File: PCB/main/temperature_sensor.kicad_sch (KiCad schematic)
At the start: 6 parts, among them Q1 FDS6690A, U1 MCP9700T-ETT

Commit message: Add sheet properties
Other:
- company: (none) -> University of Cape Town
- title: (none) -> Temperature Sensor
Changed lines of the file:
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@@
 (kicad_sch (version 20211123) (generator eeschema)
   (paper "A4")
+  (title_block
+    (title "Temperature Sensor")
+    (date "2022-03-09")
+    (rev "v1.0")
+    (company "University of Cape Town")
+    (comment 4 "Author: Kelvin Yankey")
+  )
   (junction (at 114.3 135.89) (diameter 0) (color 0 0 0 0)
   )

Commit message: Add changes
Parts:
- renumbered D4 to D10, R8 to R14, R10 to R15, R11 to R16, U1 to U7
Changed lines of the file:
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@@
   (symbol (lib_id "Device:R") (at 186.69 86.36 0) (unit 1)
     (in_bom yes) (on_board yes) (fields_autoplaced)
-    (property "Reference" "R11" (id 0) (at 189.23 85.0899 0)
+    (property "Reference" "R16" (id 0) (at 189.23 85.0899 0)
       (effects (font (size 1.27 1.27)) (justify left))
     )
@@
   (symbol (lib_id "Device:LED") (at 186.69 99.06 90) (unit 1)
     (in_bom yes) (on_board yes) (fields_autoplaced)
-    (property "Reference" "D4" (id 0) (at 190.5 99.3774 90)
+    (property "Reference" "D10" (id 0) (at 190.5 99.3774 90)
       (effects (font (size 1.27 1.27)) (justify right))
     )
@@
   (symbol (lib_id "Sensor_Temperature:MCP9700T-ETT") (at 165.1 74.93 0) (unit 1)
     (in_bom yes) (on_board yes) (fields_autoplaced)
-    (property "Reference" "U1" (id 0) (at 156.21 73.6599 0)
+    (property "Reference" "U7" (id 0) (at 156.21 73.6599 0)
       (effects (font (size 1.27 1.27)) (justify right))
     )
@@
   (symbol (lib_id "Device:R") (at 146.05 41.91 0) (unit 1)
     (in_bom yes) (on_board yes) (fields_autoplaced)
-    (property "Reference" "R8" (id 0) (at 148.59 40.6399 0)
+    (property "Reference" "R14" (id 0) (at 148.59 40.6399 0)
       (effects (font (size 1.27 1.27)) (justify left))
     )
@@
   (symbol (lib_id "Device:R") (at 146.05 53.34 0) (unit 1)
     (in_bom yes) (on_board yes) (fields_autoplaced)
-    (property "Reference" "R10" (id 0) (at 148.59 52.0699 0)
+    (property "Reference" "R15" (id 0) (at 148.59 52.0699 0)
       (effects (font (size 1.27 1.27)) (justify left))
     )

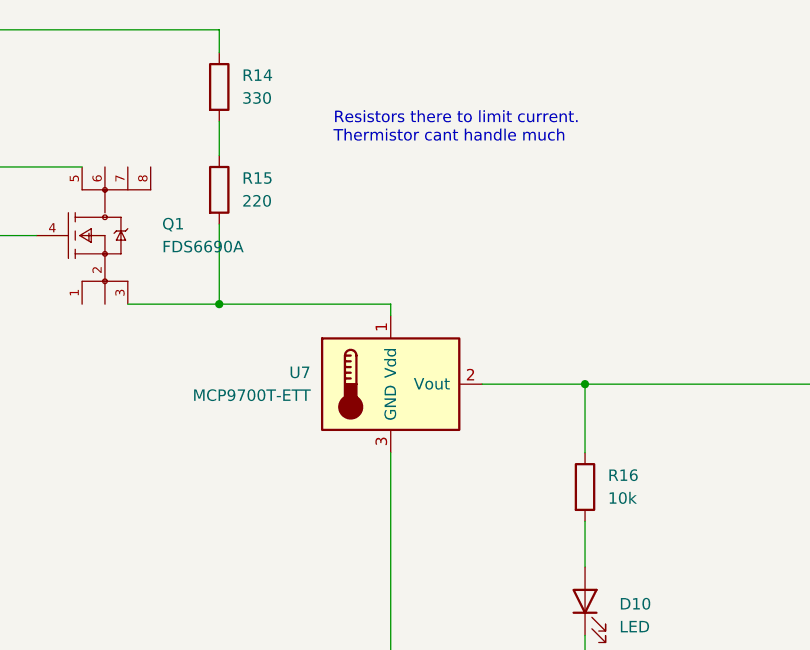
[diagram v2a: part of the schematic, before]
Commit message: Add usb sensing
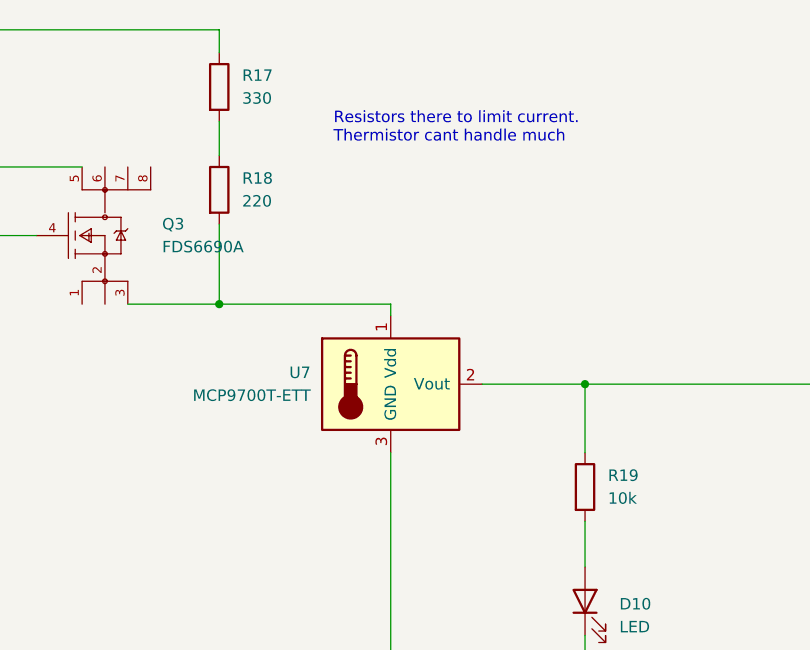
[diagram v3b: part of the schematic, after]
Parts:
- renumbered Q1 to Q3, R14 to R17, R15 to R18, R16 to R19
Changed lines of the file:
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@@
   (symbol (lib_id "Device:R") (at 186.69 86.36 0) (unit 1)
     (in_bom yes) (on_board yes) (fields_autoplaced)
-    (property "Reference" "R16" (id 0) (at 189.23 85.0899 0)
+    (property "Reference" "R19" (id 0) (at 189.23 85.0899 0)
       (effects (font (size 1.27 1.27)) (justify left))
     )
@@
   (symbol (lib_id "Symbol_EEE3088F:FDS6690A") (at 123.19 58.42 0) (unit 1)
     (in_bom yes) (on_board yes) (fields_autoplaced)
-    (property "Reference" "Q1" (id 0) (at 139.7 57.1499 0)
+    (property "Reference" "Q3" (id 0) (at 139.7 57.1499 0)
       (effects (font (size 1.27 1.27)) (justify left))
     )
@@
   (symbol (lib_id "Device:R") (at 146.05 41.91 0) (unit 1)
     (in_bom yes) (on_board yes) (fields_autoplaced)
-    (property "Reference" "R14" (id 0) (at 148.59 40.6399 0)
+    (property "Reference" "R17" (id 0) (at 148.59 40.6399 0)
       (effects (font (size 1.27 1.27)) (justify left))
     )
@@
   (symbol (lib_id "Device:R") (at 146.05 53.34 0) (unit 1)
     (in_bom yes) (on_board yes) (fields_autoplaced)
-    (property "Reference" "R15" (id 0) (at 148.59 52.0699 0)
+    (property "Reference" "R18" (id 0) (at 148.59 52.0699 0)
       (effects (font (size 1.27 1.27)) (justify left))
     )

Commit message: Final Changes
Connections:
- no-connect marks 0 -> 5
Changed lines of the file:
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@@
   (junction (at 146.05 66.04) (diameter 0) (color 0 0 0 0)
   )
+  (no_connect (at 133.35 66.04))
+  (no_connect (at 130.81 66.04))
+  (no_connect (at 133.35 50.8))
+  (no_connect (at 135.89 50.8))
+  (no_connect (at 138.43 50.8))
   (bus_entry (at 152.4 140.97) (size 2.54 2.54)
     (stroke (width 0) (type default) (color 0 0 0 0))

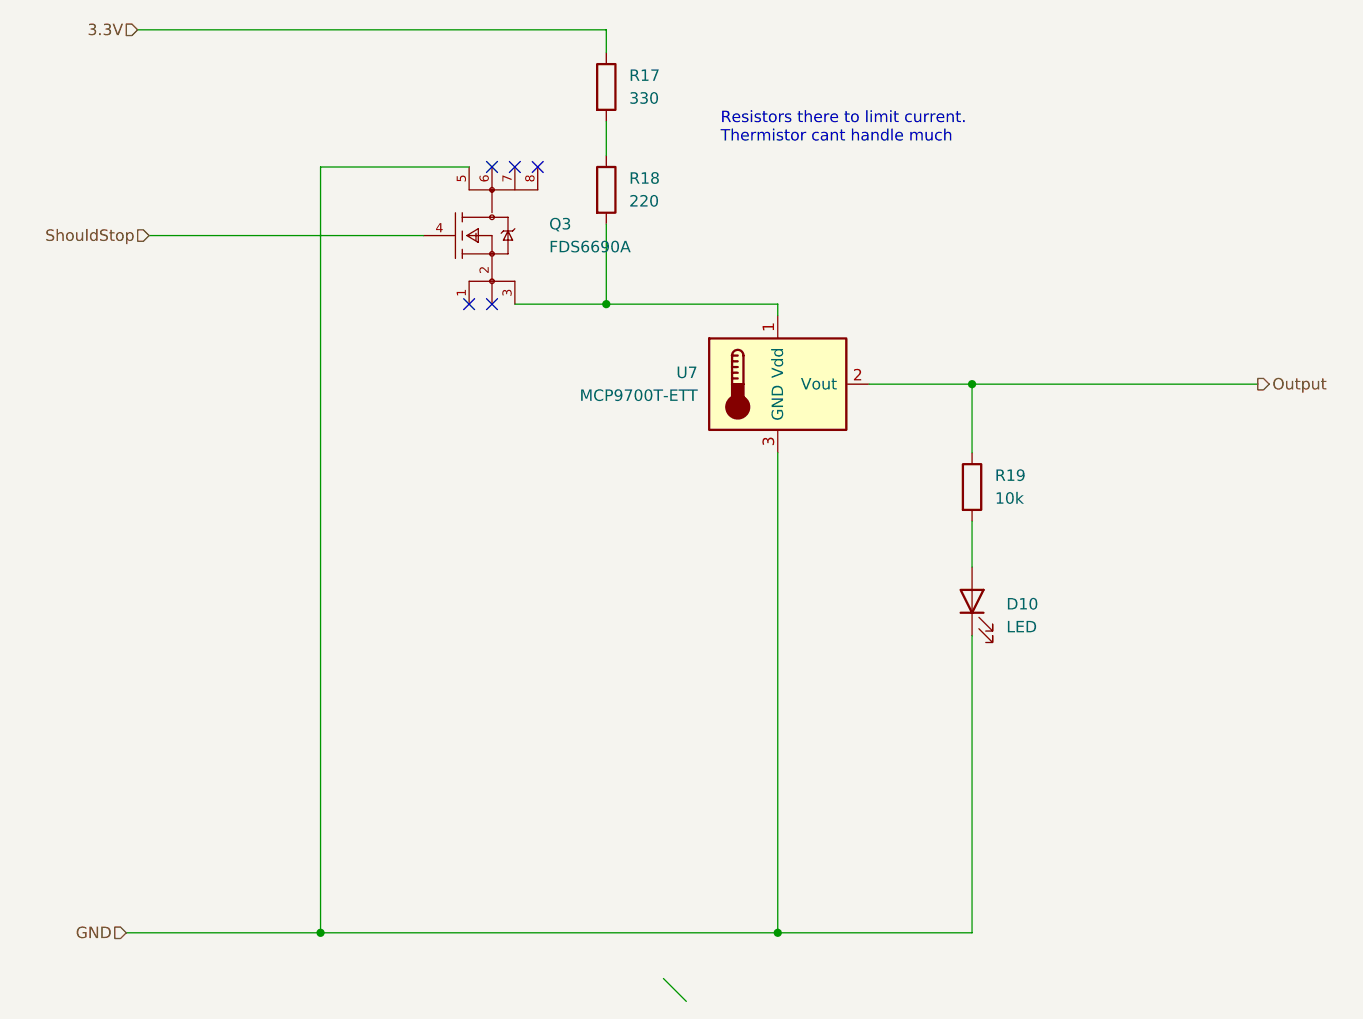
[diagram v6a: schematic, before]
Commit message: Fixed incorrect connection for MOSFET in Sensing Subsystem \n\n Since the BJT switch has been replaced by a MOSFET switch, the Should Stop pin in the temperature sensor should become an Active pin. Indicating when the system should be on
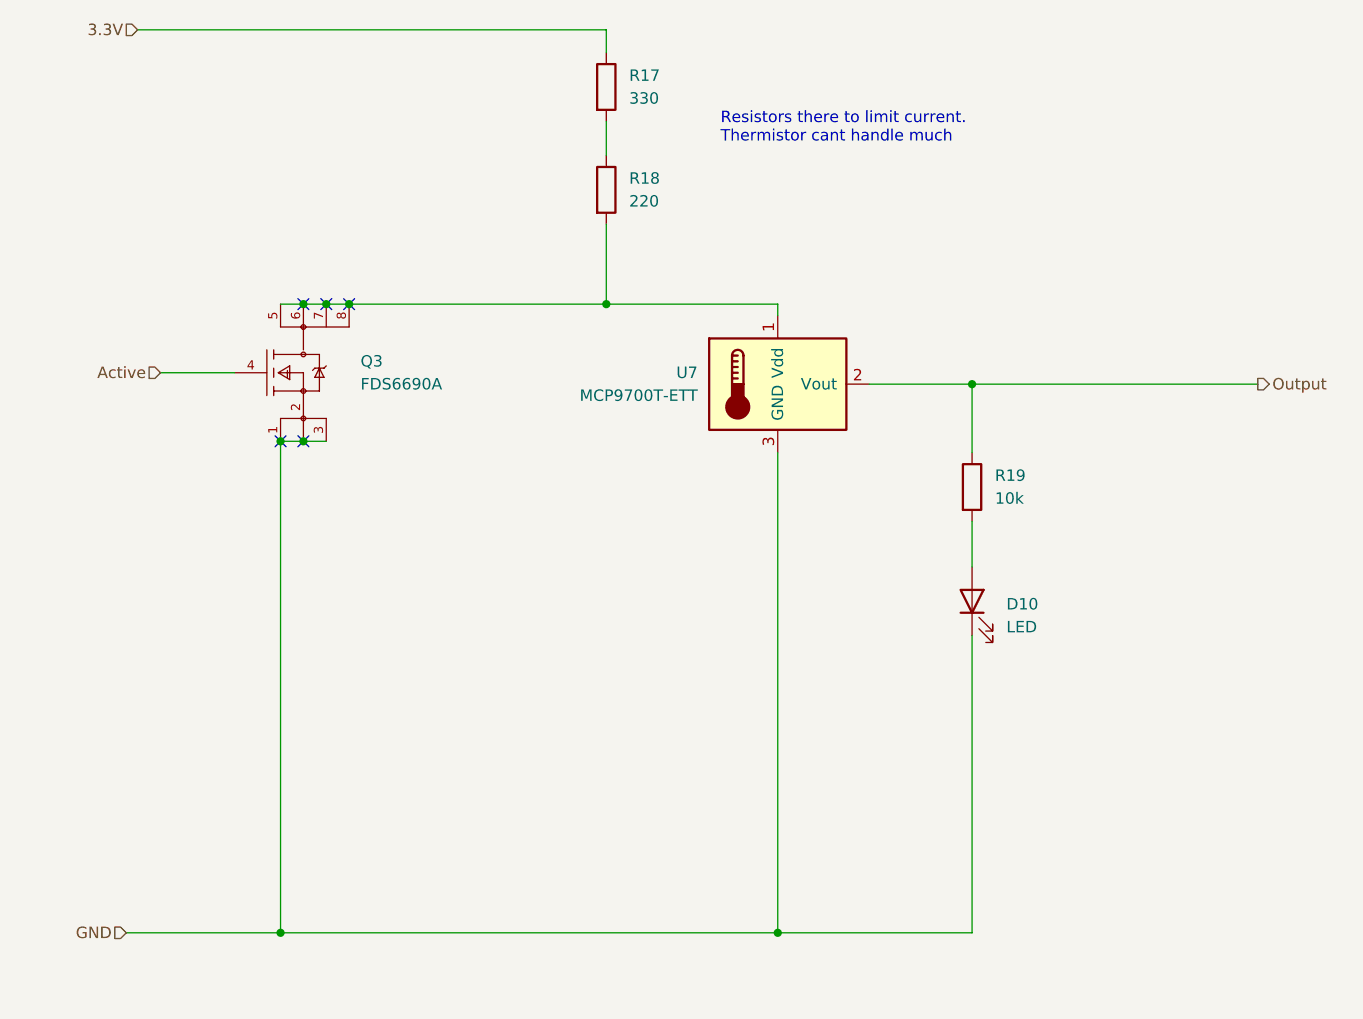
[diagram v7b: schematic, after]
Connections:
- net GND: now also Q3.1 (S), Q3.2 (S), Q3.3 (S); no longer Q3.5 (D)
- net at R18.2, U7.1 (Vdd): now also Q3.5 (D), Q3.6 (D), Q3.7 (D), Q3.8 (D); no longer Q3.3 (S)
- net ShouldStop renamed Active
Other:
- moved on the sheet: Q3
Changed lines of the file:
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@@
     (comment 4 "Author: Kelvin Yankey")
   )
-  (junction (at 114.3 135.89) (diameter 0) (color 0 0 0 0)
+  (junction (at 146.05 66.04) (diameter 0) (color 0 0 0 0)
+  )
+  (junction (at 114.935 66.04) (diameter 0) (color 0 0 0 0)
+  )
+  (junction (at 112.395 81.28) (diameter 0) (color 0 0 0 0)
   )
   (junction (at 186.69 74.93) (diameter 0) (color 0 0 0 0)
   )
+  (junction (at 109.855 135.89) (diameter 0) (color 0 0 0 0)
+  )
+  (junction (at 112.395 66.04) (diameter 0) (color 0 0 0 0)
+  )
   (junction (at 165.1 135.89) (diameter 0) (color 0 0 0 0)
   )
-  (junction (at 146.05 66.04) (diameter 0) (color 0 0 0 0)
-  )
-  (no_connect (at 133.35 66.04))
-  (no_connect (at 130.81 66.04))
-  (no_connect (at 133.35 50.8))
-  (no_connect (at 135.89 50.8))
-  (no_connect (at 138.43 50.8))
-  (bus_entry (at 152.4 140.97) (size 2.54 2.54)
+  (junction (at 109.855 81.28) (diameter 0) (color 0 0 0 0)
+  )
+  (junction (at 117.475 66.04) (diameter 0) (color 0 0 0 0)
+  )
+  (no_connect (at 112.395 81.28))
+  (no_connect (at 109.855 81.28))
+  (no_connect (at 112.395 66.04))
+  (no_connect (at 114.935 66.04))
+  (no_connect (at 117.475 66.04))
+  (wire (pts (xy 109.855 81.28) (xy 109.855 135.89))
+    (stroke (width 0) (type default) (color 0 0 0 0))
+  )
+  (wire (pts (xy 92.71 135.89) (xy 109.855 135.89))
     (stroke (width 0) (type default) (color 0 0 0 0))
   )
@@
     (stroke (width 0) (type default) (color 0 0 0 0))
   )
+  (wire (pts (xy 117.475 66.04) (xy 146.05 66.04))
+    (stroke (width 0) (type default) (color 0 0 0 0))
+  )
   (wire (pts (xy 175.26 74.93) (xy 186.69 74.93))
     (stroke (width 0) (type default) (color 0 0 0 0))
@@
     (stroke (width 0) (type default) (color 0 0 0 0))
   )
-  (wire (pts (xy 92.71 135.89) (xy 114.3 135.89))
+  (wire (pts (xy 114.935 66.04) (xy 117.475 66.04))
     (stroke (width 0) (type default) (color 0 0 0 0))
   )
@@
     (stroke (width 0) (type default) (color 0 0 0 0))
   )
+  (wire (pts (xy 96.52 73.66) (xy 104.775 73.66))
+    (stroke (width 0) (type default) (color 0 0 0 0))
+  )
   (wire (pts (xy 186.69 90.17) (xy 186.69 95.25))
     (stroke (width 0) (type default) (color 0 0 0 0))
   )
-  (wire (pts (xy 114.3 135.89) (xy 165.1 135.89))
-    (stroke (width 0) (type default) (color 0 0 0 0))
-  )
-  (wire (pts (xy 130.81 50.8) (xy 114.3 50.8))
+  (wire (pts (xy 109.855 81.28) (xy 112.395 81.28))
     (stroke (width 0) (type default) (color 0 0 0 0))
   )
@@
     (stroke (width 0) (type default) (color 0 0 0 0))
   )
-  (wire (pts (xy 95.25 58.42) (xy 125.73 58.42))
+  (wire (pts (xy 109.855 66.04) (xy 112.395 66.04))
     (stroke (width 0) (type default) (color 0 0 0 0))
   )
@@
     (stroke (width 0) (type default) (color 0 0 0 0))
   )
-  (wire (pts (xy 114.3 50.8) (xy 114.3 135.89))
+  (wire (pts (xy 109.855 135.89) (xy 165.1 135.89))
+    (stroke (width 0) (type default) (color 0 0 0 0))
+  )
+  (wire (pts (xy 112.395 66.04) (xy 114.935 66.04))
+    (stroke (width 0) (type default) (color 0 0 0 0))
+  )
+  (wire (pts (xy 112.395 81.28) (xy 114.935 81.28))
     (stroke (width 0) (type default) (color 0 0 0 0))
   )
@@
   )
   (wire (pts (xy 146.05 66.04) (xy 165.1 66.04))
-    (stroke (width 0) (type default) (color 0 0 0 0))
-  )
-  (wire (pts (xy 135.89 66.04) (xy 146.05 66.04))
     (stroke (width 0) (type default) (color 0 0 0 0))
   )
@@
     (effects (font (size 1.27 1.27)) (justify left bottom))
   )
-  (hierarchical_label "ShouldStop" (shape input) (at 95.25 58.42 180)
+  (hierarchical_label "Active" (shape input) (at 96.52 73.66 180)
     (effects (font (size 1.27 1.27)) (justify right))
   )
@@
     (pin "2")
   )
-  (symbol (lib_id "Symbol_EEE3088F:FDS6690A") (at 123.19 58.42 0) (unit 1)
-    (in_bom yes) (on_board yes) (fields_autoplaced)
-    (property "Reference" "Q3" (id 0) (at 139.7 57.1499 0)
-      (effects (font (size 1.27 1.27)) (justify left))
-    )
-    (property "Value" "FDS6690A" (id 1) (at 139.7 59.6899 0)
-      (effects (font (size 1.27 1.27)) (justify left))
-    )
-    (property "Footprint" "ON_Semi-CASE_751EB-0-0-*" (id 2) (at 123.19 43.18 0)
-      (effects (font (size 1.27 1.27)) (justify left) hide)
-    )
-    (property "Datasheet" "https://datasheet.lcsc.com/lcsc/1912111437_ON-Semiconductor-FDS6690A_C87667.pdf" (id 3) (at 123.19 40.64 0)
-      (effects (font (size 1.27 1.27)) (justify left) hide)
-    )
-    (property "category" "Trans" (id 4) (at 123.19 38.1 0)
-      (effects (font (size 1.27 1.27)) (justify left) hide)
-    )
-    (property "digikey description" "N-Channel 30V 11A (Ta) 2.5W (Ta) Surface Mount 8-SO" (id 5) (at 123.19 35.56 0)
-      (effects (font (size 1.27 1.27)) (justify left) hide)
-    )
-    (property "digikey part number" "FDS6690ACT-ND" (id 6) (at 123.19 33.02 0)
-      (effects (font (size 1.27 1.27)) (justify left) hide)
-    )
-    (property "lead free" "yes" (id 7) (at 123.19 30.48 0)
-      (effects (font (size 1.27 1.27)) (justify left) hide)
-    )
-    (property "library id" "f343f3e1ec73a186" (id 8) (at 123.19 27.94 0)
-      (effects (font (size 1.27 1.27)) (justify left) hide)
-    )
-    (property "manufacturer" "ON Semi" (id 9) (at 123.19 25.4 0)
-      (effects (font (size 1.27 1.27)) (justify left) hide)
-    )
-    (property "mouser part number" "512-FDS6690A" (id 10) (at 123.19 22.86 0)
-      (effects (font (size 1.27 1.27)) (justify left) hide)
-    )
-    (property "package" "SO8" (id 11) (at 123.19 20.32 0)
-      (effects (font (size 1.27 1.27)) (justify left) hide)
-    )
-    (property "rohs" "yes" (id 12) (at 123.19 17.78 0)
-      (effects (font (size 1.27 1.27)) (justify left) hide)
-    )
-    (property "temperature range high" "+150°C" (id 13) (at 123.19 15.24 0)
-      (effects (font (size 1.27 1.27)) (justify left) hide)
-    )
-    (property "temperature range low" "-55°C" (id 14) (at 123.19 12.7 0)
-      (effects (font (size 1.27 1.27)) (justify left) hide)
-    )
-    (property "JLCPart" " C87667 " (id 15) (at 123.19 58.42 0)
-      (effects (font (size 1.27 1.27)) hide)
-    )
+  (symbol (lib_id "Symbol_EEE3088F:FDS6690A") (at 102.235 73.66 0) (unit 1)
+    (in_bom yes) (on_board yes) (fields_autoplaced)
+    (property "Reference" "Q3" (id 0) (at 118.745 72.3899 0)
+      (effects (font (size 1.27 1.27)) (justify left))
+    )
+    (property "Value" "FDS6690A" (id 1) (at 118.745 74.9299 0)
+      (effects (font (size 1.27 1.27)) (justify left))
+    )
+    (property "Footprint" "ON_Semi-CASE_751EB-0-0-*" (id 2) (at 102.235 58.42 0)
+      (effects (font (size 1.27 1.27)) (justify left) hide)
+    )
+    (property "Datasheet" "https://datasheet.lcsc.com/lcsc/1912111437_ON-Semiconductor-FDS6690A_C87667.pdf" (id 3) (at 102.235 55.88 0)
+      (effects (font (size 1.27 1.27)) (justify left) hide)
+    )
+    (property "category" "Trans" (id 4) (at 102.235 53.34 0)
+      (effects (font (size 1.27 1.27)) (justify left) hide)
+    )
+    (property "digikey description" "N-Channel 30V 11A (Ta) 2.5W (Ta) Surface Mount 8-SO" (id 5) (at 102.235 50.8 0)
+      (effects (font (size 1.27 1.27)) (justify left) hide)
+    )
+    (property "digikey part number" "FDS6690ACT-ND" (id 6) (at 102.235 48.26 0)
+      (effects (font (size 1.27 1.27)) (justify left) hide)
+    )
+    (property "lead free" "yes" (id 7) (at 102.235 45.72 0)
+      (effects (font (size 1.27 1.27)) (justify left) hide)
+    )
+    (property "library id" "f343f3e1ec73a186" (id 8) (at 102.235 43.18 0)
+      (effects (font (size 1.27 1.27)) (justify left) hide)
+    )
+    (property "manufacturer" "ON Semi" (id 9) (at 102.235 40.64 0)
+      (effects (font (size 1.27 1.27)) (justify left) hide)
+    )
+    (property "mouser part number" "512-FDS6690A" (id 10) (at 102.235 38.1 0)
+      (effects (font (size 1.27 1.27)) (justify left) hide)
+    )
+    (property "package" "SO8" (id 11) (at 102.235 35.56 0)
+      (effects (font (size 1.27 1.27)) (justify left) hide)
+    )
+    (property "rohs" "yes" (id 12) (at 102.235 33.02 0)
+      (effects (font (size 1.27 1.27)) (justify left) hide)
+    )
+    (property "temperature range high" "+150°C" (id 13) (at 102.235 30.48 0)
+      (effects (font (size 1.27 1.27)) (justify left) hide)
+    )
+    (property "temperature range low" "-55°C" (id 14) (at 102.235 27.94 0)
+      (effects (font (size 1.27 1.27)) (justify left) hide)
+    )
+    (property "JLCPart" " C87667 " (id 15) (at 102.235 73.66 0)
+      (effects (font (size 1.27 1.27)) hide)
+    )
